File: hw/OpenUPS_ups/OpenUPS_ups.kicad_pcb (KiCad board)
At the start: 4 copper layers, 90 x 62 mm, 287 parts, among them J1001 USB4105-GF-A, J101 Barrel Jack, J102 XT30PW-M, J103 XT30PW-M, J104 S2B-PH-K_1x02, J105 S2B-PH-K_1x02, J106 Screw Terminal, J107 Screw Terminal, J108 Screw Terminal, J109 JST XH, J110 JST XH, J501 Conn_01x03, J701 0022053031, J702 0022053031, J901 Qwiic, J902 Qwiic, Q1001 2N7002, Q301 AON7534, Q302 AON7534, Q303 AON7534, Q304 AON7534, Q401 2N7002, Q402 AON7534, Q403 AON7534, Q404 AON7534, Q405 AON7534, Q601 AON7534, Q602 AON7534, Q603 AON7534, Q604 AON7534, Q701 2N7002, Q702 2N7002, U1001 MCP6547, U1002 AP22814BW5, U1003 NUP2301MW6T1G, U101 AVR32DB48x-xPT, U102 NUP2301MW6T1G, U103 LM75BTP,147, U201 TPS51397A, U202 INA180A3, U301 NCP81599, U401 NCP431, U402 BD99950, U403 MCP6001R, U404 DZDH0401DW, U405 INA180A1, U601 NCP81599, U701 NUP2301MW6T1G, U702 NUP2301MW6T1G, U801 AP7383-33W5, U901 π220N31

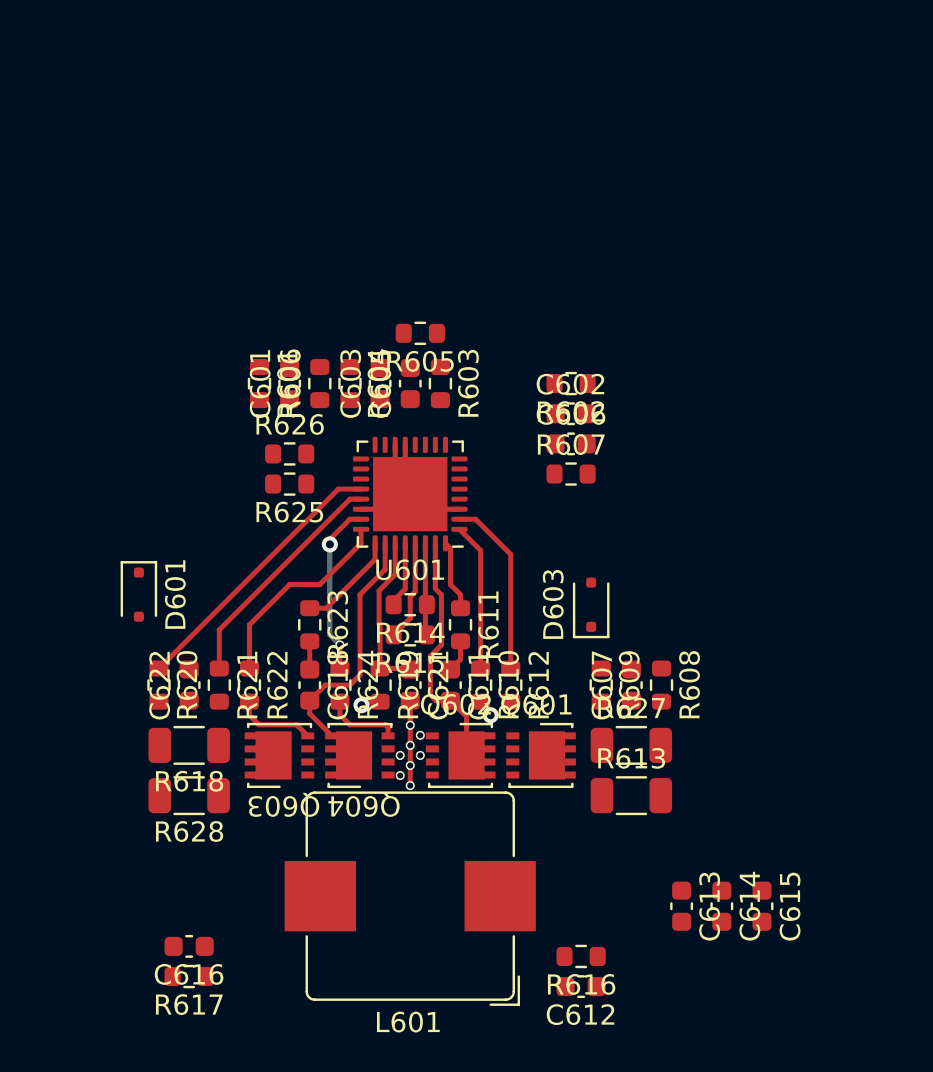
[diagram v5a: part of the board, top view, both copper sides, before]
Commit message: Applied design rules to PCB editor #28
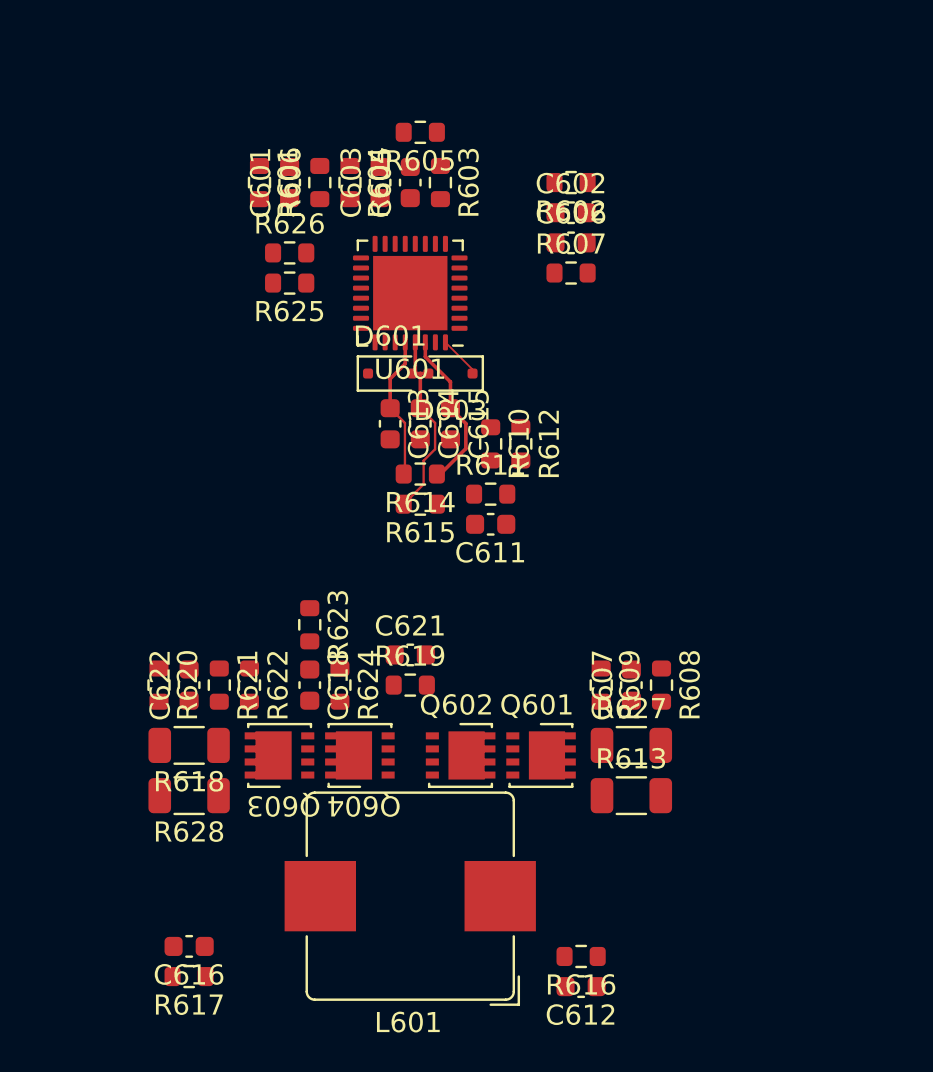
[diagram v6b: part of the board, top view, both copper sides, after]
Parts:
- moved C615 28.6 mm to (46.5, 159.5)
- moved C614 28.3 mm to (45.0, 159.5)
- moved C613 28.0 mm to (43.5, 159.5)
- moved D601 16.7 mm to (43.5, 157.0), turned to 0 degrees
- moved D603 13.5 mm to (46.5, 157.0), turned to 180 degrees
- moved R610 12.0 mm to (48.5, 160.5)
- moved R612 12.0 mm to (50.0, 160.5)
- moved C601 10.0 mm to (38.5, 147.5)
- moved C602 10.0 mm to (52.5, 149.0)
- moved C603 10.0 mm to (43.0, 147.5)
- moved C605 10.0 mm to (44.5, 147.5)
- moved C606 10.0 mm to (52.5, 150.5)
- moved R601 10.0 mm to (37.0, 147.5)
- moved R602 10.0 mm to (52.5, 147.5)
- moved R603 10.0 mm to (46.0, 147.5)
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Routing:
- net GND: track 18.4 -> 3.34 mm, vias 4 -> 0
- net Net-(U601C-CSN2): track 13.7 -> 0.00 mm
- net Net-(U601C-VSW2): track 12.3 -> 0.00 mm
- net Net-(U601B-VSW1): track 12.1 -> 0.00 mm
- net Net-(U601C-CSP2): track 11.7 -> 0.00 mm
- net Net-(U601C-HSG2): track 10.1 -> 0.00 mm
- net Net-(U601B-LSG1): track 8.95 -> 0.00 mm
- net Net-(U601C-LSG2): track 8.60 -> 0.00 mm, vias 6 -> 0
- net Net-(U601C-V2): track 8.10 -> 0.00 mm
- net Net-(U601B-HSG1): track 7.36 -> 0.00 mm
- net Net-(D601-K): track 5.05 -> 0.00 mm
- net /12V Buck_Boost/VDRV: track 5.00 -> 9.86 mm
- net Net-(Q603-G): track 4.00 -> 0.00 mm
- net Net-(U601A-VCCD): track 3.29 -> 7.19 mm
- net Net-(Q604-G): track 3.73 -> 0.00 mm
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
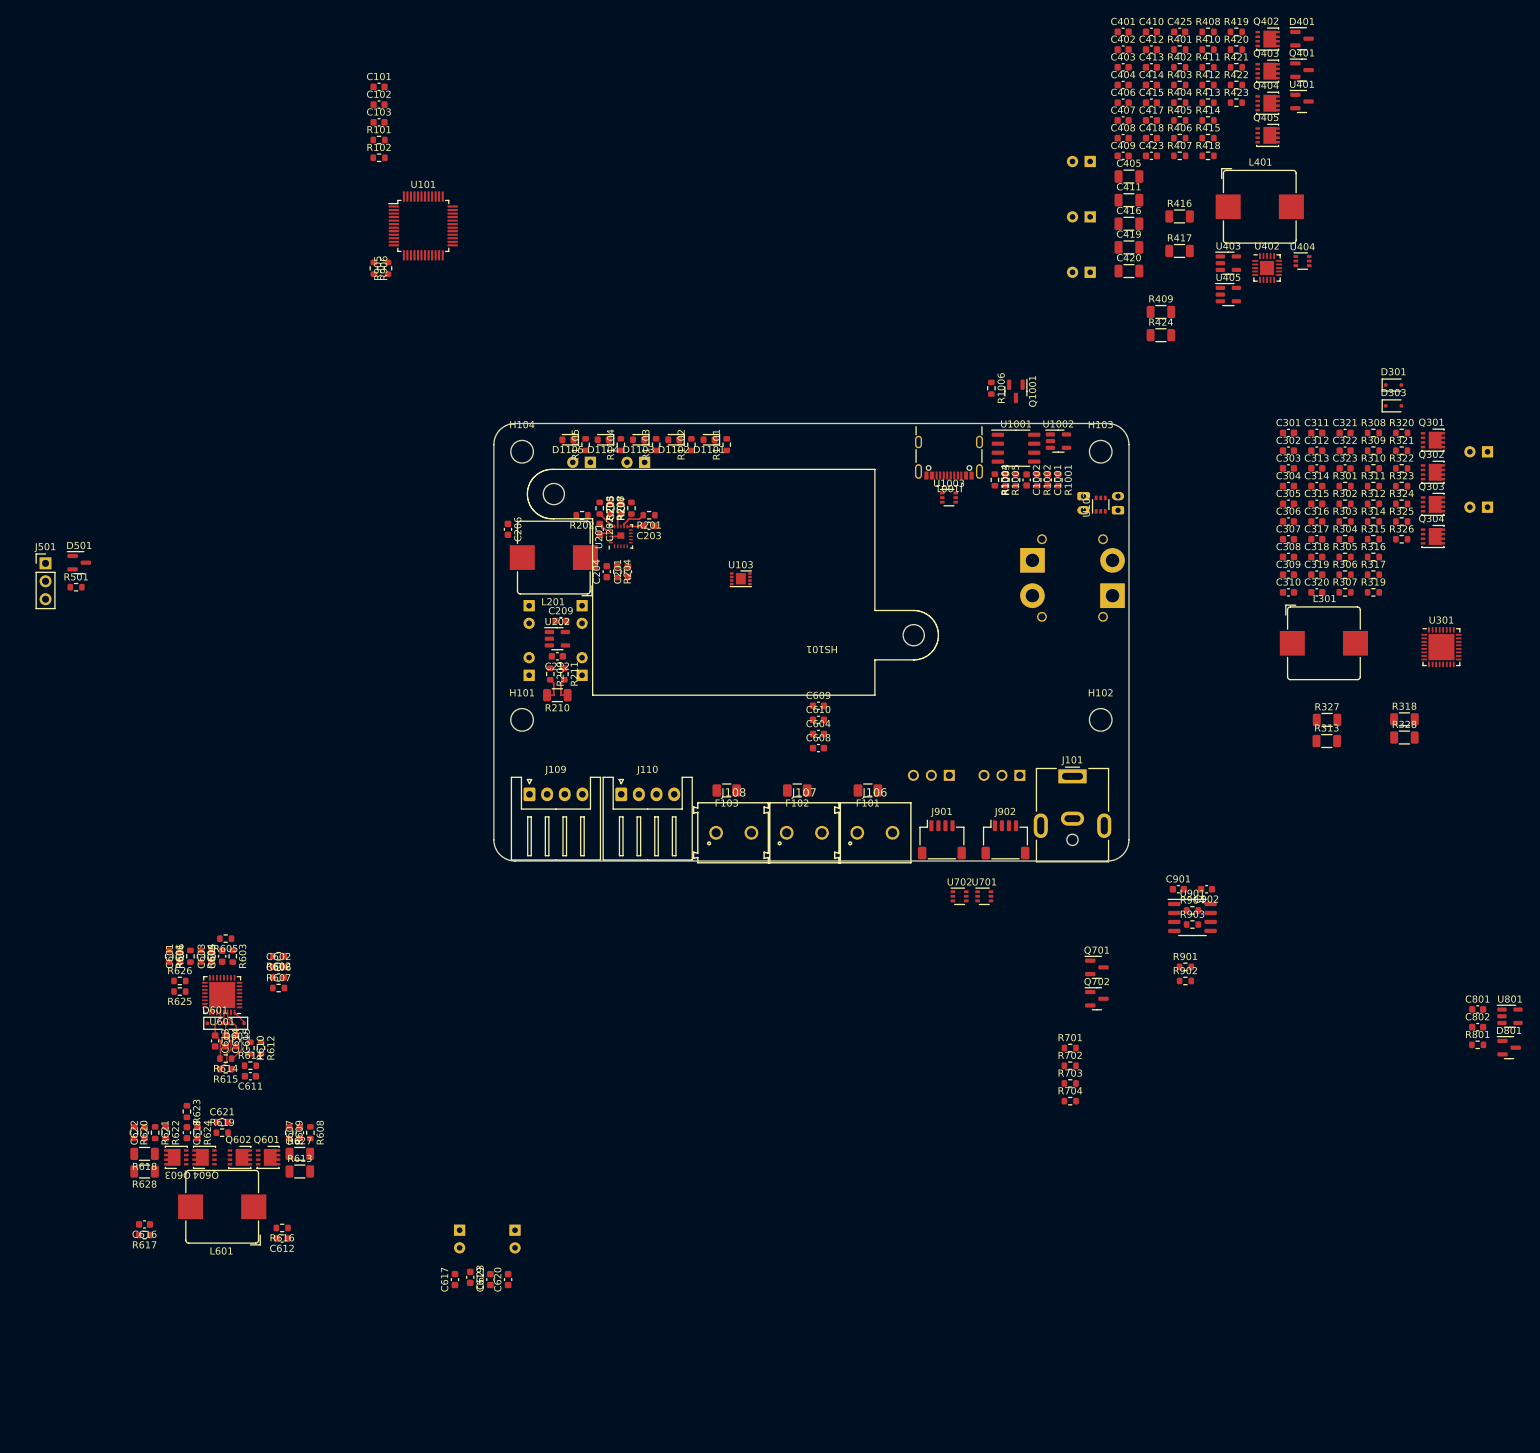
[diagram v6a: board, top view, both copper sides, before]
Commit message: 12V converter layout
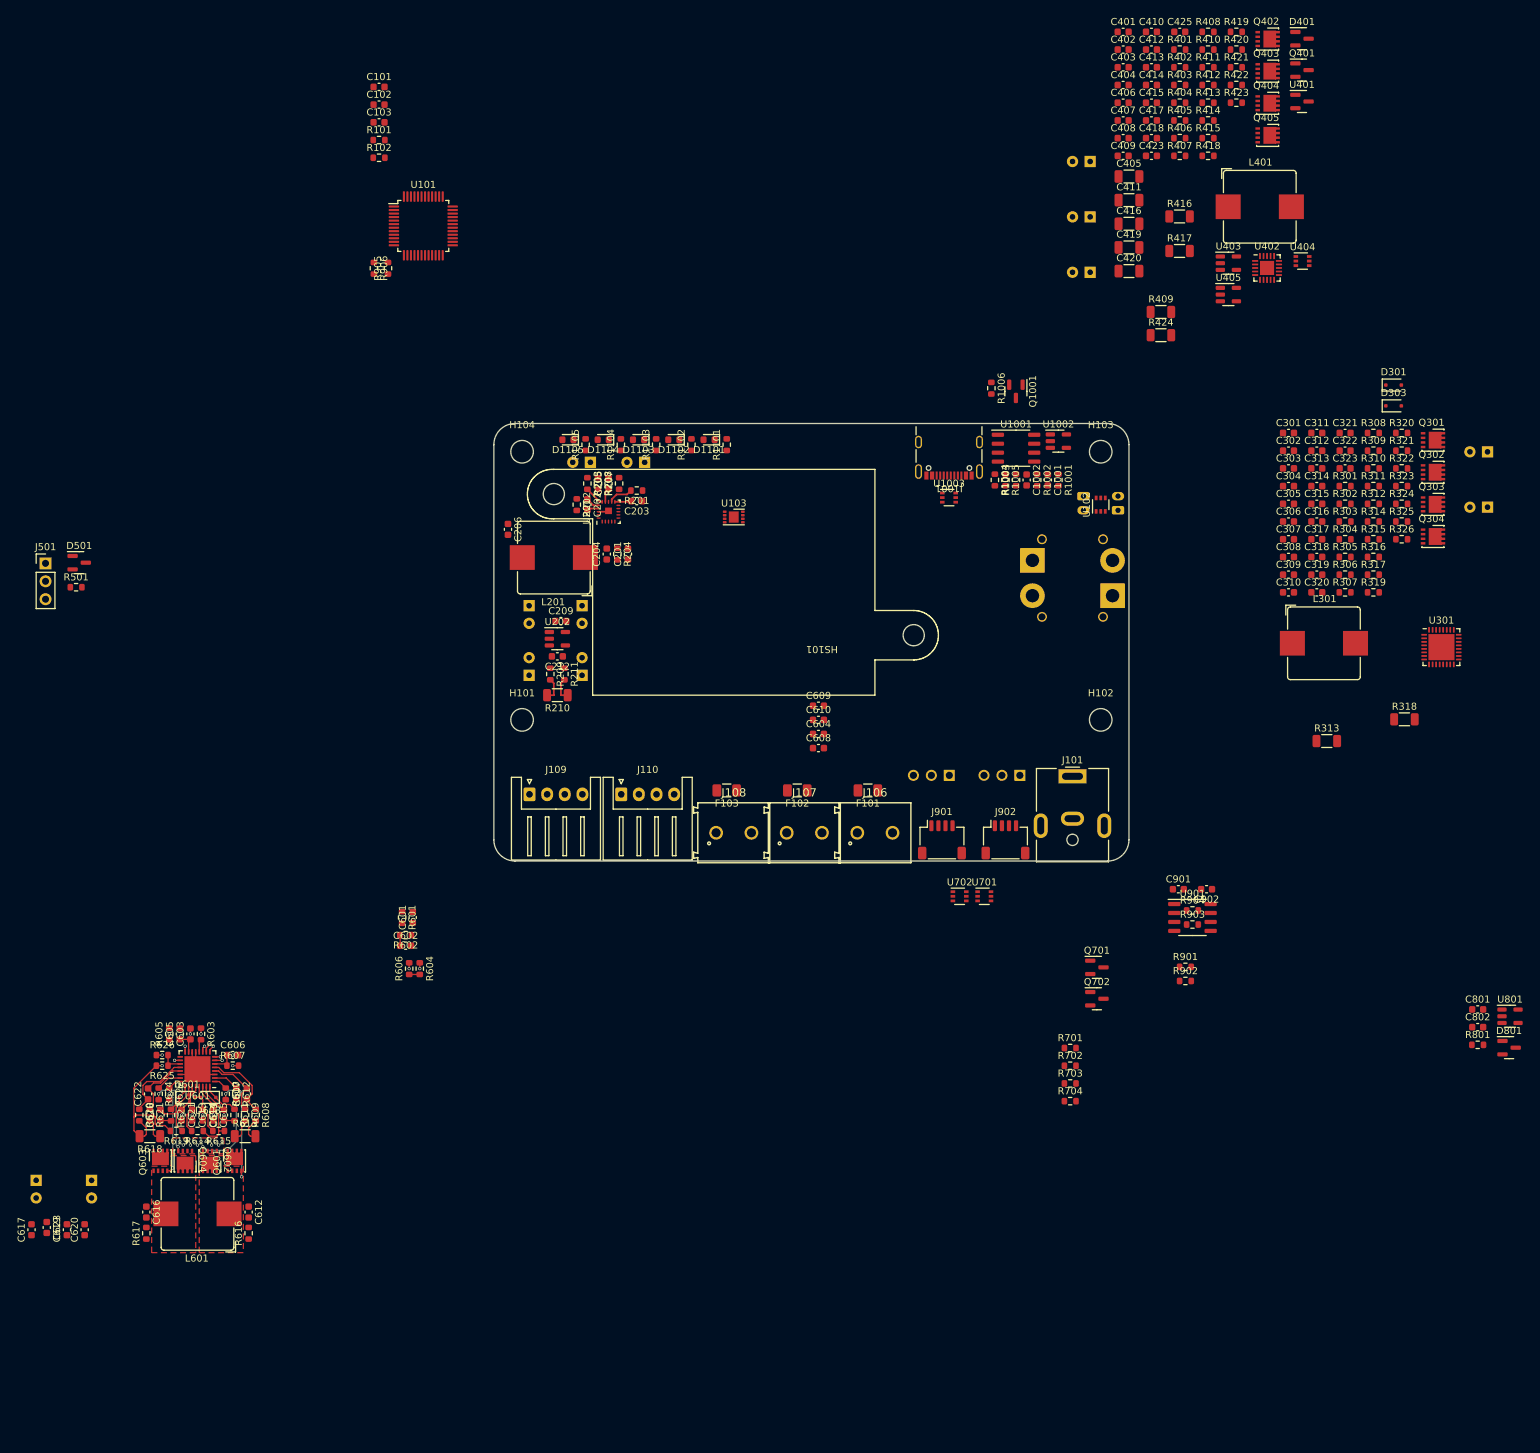
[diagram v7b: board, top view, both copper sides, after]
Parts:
- removed R327, R328, R627, R628: 10m 1/2W, Resistor_SMD:R_1206_3216Metric
- R313, R318, R613, R618: value 10m 1/2W -> 5m 1W
- moved C619 60.4 mm to (22.5, 186.2)
- moved C623 60.4 mm to (19.6, 185.9)
- moved C624 60.4 mm to (18.1, 179.2)
- moved C625 60.4 mm to (26.0, 179.2)
- moved C617 60.4 mm to (17.5, 186.2)
- moved C620 60.4 mm to (25.0, 186.2)
- moved C601 33.5 mm to (71.5, 142.0)
- moved R601 33.5 mm to (70.0, 142.0)
- moved R604 31.0 mm to (72.5, 149.2)
- moved R606 31.0 mm to (71.0, 149.2)
- moved C602 18.2 mm to (70.5, 146.0)
- moved R602 18.2 mm to (70.5, 144.5)
- moved R605 15.7 mm to (37.0, 158.5), turned to 90 degrees
- moved C606 12.8 mm to (46.0, 161.5)
- moved R607 12.8 mm to (46.0, 163.0)
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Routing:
- net +12V: track 0.00 -> 22.7 mm, vias 0 -> 1
- net GND: track 3.34 -> 22.1 mm, vias 0 -> 10
- net Net-(Q601-G): track 0.00 -> 16.2 mm, vias 0 -> 2
- net Net-(Q602-G): track 0.00 -> 13.7 mm, vias 0 -> 2
- net Net-(Q603-G): track 0.00 -> 12.5 mm, vias 0 -> 2
- net Net-(Q604-G): track 0.00 -> 12.1 mm, vias 0 -> 2
- net Net-(U601B-CSP1): track 0.00 -> 10.6 mm
- net Net-(U601C-CSN2): track 0.00 -> 10.5 mm
- net Net-(U601C-CSP2): track 0.00 -> 9.04 mm
- net Net-(U601B-CSN1): track 0.00 -> 9.03 mm
- net Net-(U601C-V2): track 0.00 -> 7.56 mm
- net Net-(U601C-VSW2): track 0.00 -> 6.95 mm
- net Net-(U601B-VSW1): track 0.00 -> 5.21 mm, vias 0 -> 1
- net Vsys: track 0.00 -> 4.23 mm, vias 0 -> 1
- net Net-(D601-K): track 0.00 -> 4.05 mm
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- added copper zone on F.Cu, net GND
- added copper zone on F.Cu, net Net-(U601B-VSW1)
- added copper zone on F.Cu, net Net-(U601C-VSW2)
